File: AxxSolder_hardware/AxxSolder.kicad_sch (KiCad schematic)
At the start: 130 parts, among them IC1 OPA2387DSGT, IC3 TPS54302DDCR, IC4 STUSB4500QTR, IC5 LTC4440AHMS8E, IC6 MAX16171ATA_VY+T, IC7 STM32G431CBT6, J1 USB4110-GF-A, J2 691243110009, J3 Conn_01x05_Socket, Q1 STL9P3LLH6, Q2 2N7002NXAKR, Q3 STL10N3LLH5, U3 PEC11J-9220F-S0015, U4 BSC014N04LS

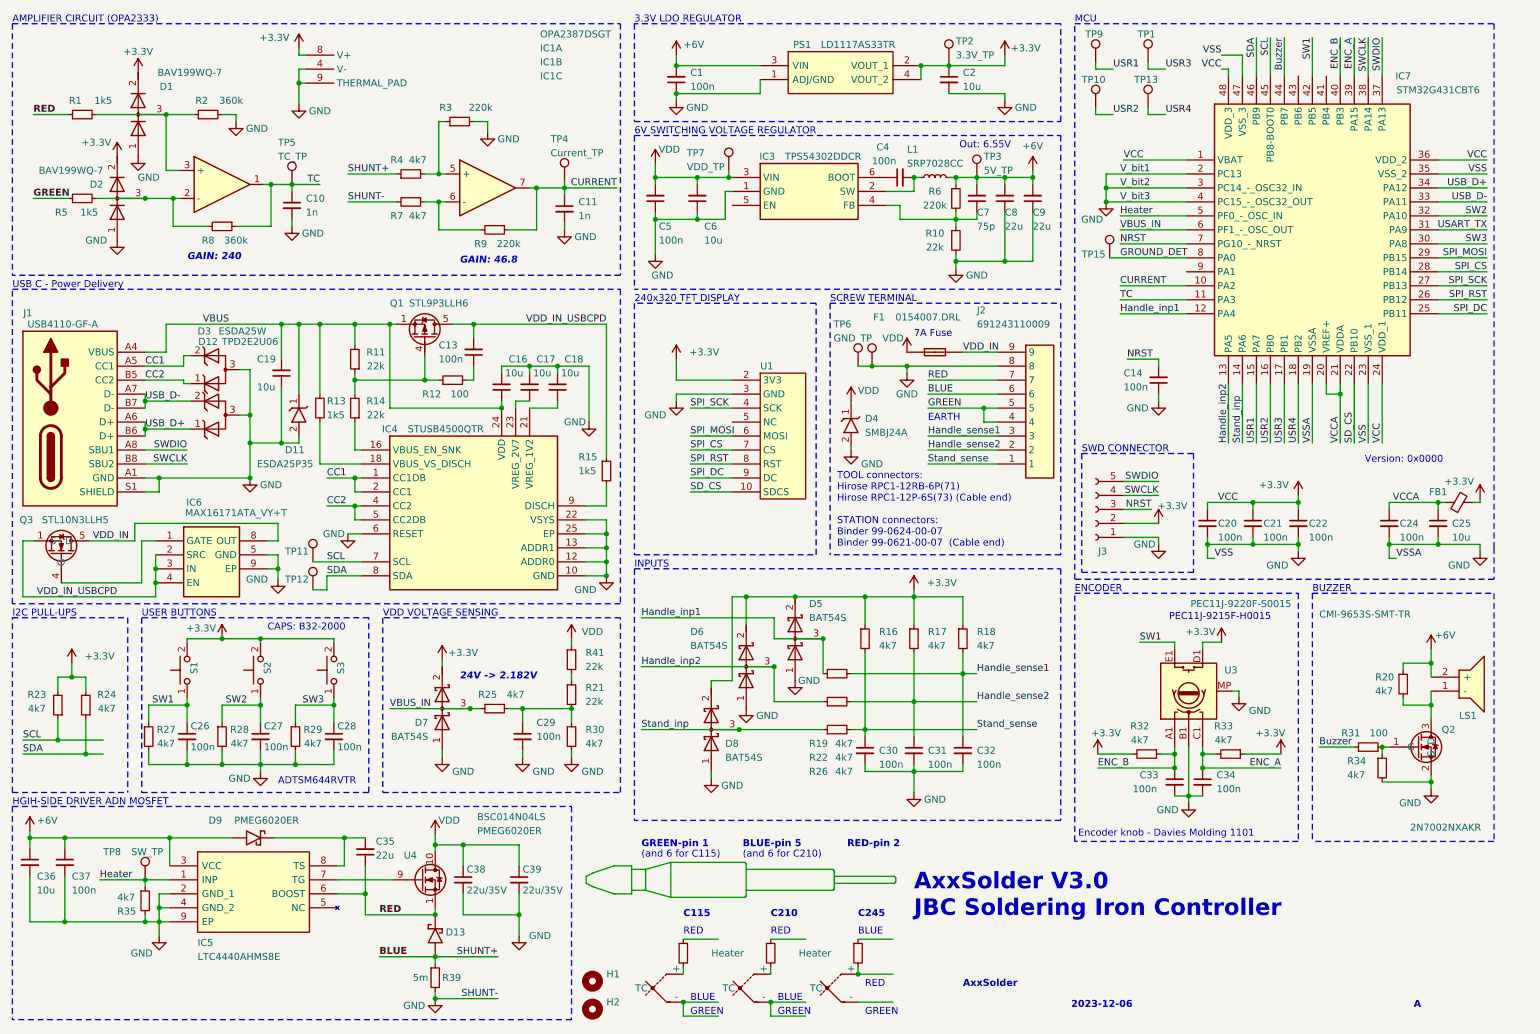
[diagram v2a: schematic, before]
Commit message: Update grounding layout and adding a fuse
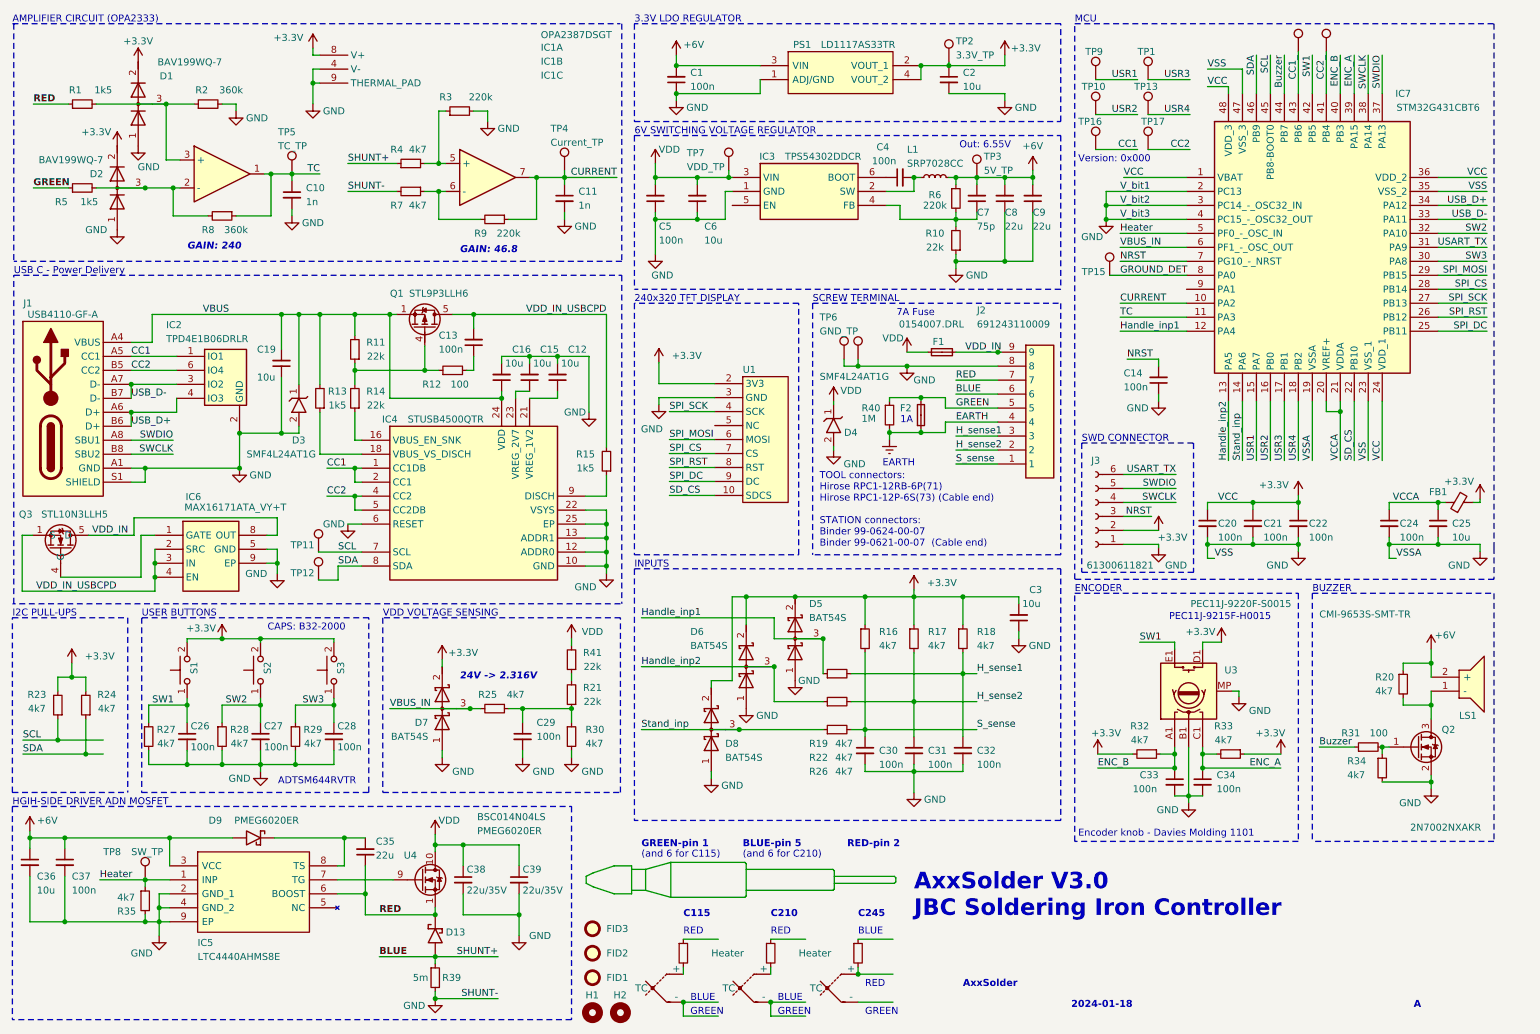
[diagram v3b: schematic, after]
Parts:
- removed C17, C18: 10u, Capacitor_SMD:C_0603_1608Metric, symbol Device:C_Small
- removed D11: ESDA25P35, footprints:ESDA25P351U1M, symbol ESDA25P35-1U1M:ESDA25P35-1U1M
- removed D12: TPD2E2U06, footprints:SOT95P237X95-3N, symbol TPD2E2U06QDBZRQ1:TPD2E2U06QDBZRQ1
- removed D3: ESDA25W, footprints:SOT65P210X110-3N, symbol ESDA25W:ESDA25W
- removed D4: SMBJ24A, footprints:DIOM5436X261N, symbol SMBJ24A:SMBJ24A
- removed J3: Conn_01x05_Socket, Connector_PinSocket_2.54mm:PinSocket_1x05_P2.54mm_Vertical, symbol Connector:Conn_01x05_Socket
- added C12, C15, C3: 10u, Capacitor_SMD:C_0603_1608Metric, symbol Device:C_Small
- added D3, D4: SMF4L24AT1G, footprints:SODFL3619X98N, symbol SMF4L24AT1G:SMF4L24AT1G
- added F2: SF-2410FP100W-2, SF2410FP100W2, symbol SF-2410FP100W-2:SF-2410FP100W-2
- added FID1, FID2, FID3: Fiducial, Fiducial:Fiducial_0.75mm_Mask1.5mm, symbol Mechanical:Fiducial
- added IC2: TPD4E1B06DRLR, footprints:SOTFL50P160X60-6N, symbol TPD4E1B06DRLR:TPD4E1B06DRLR
- added J3: 61300611821, footprints:RHDR6W97P0X254_1X6_1574X250X865P, symbol 61300611821:61300611821
- added R40: 1M, Resistor_SMD:R_1206_3216Metric, symbol Device:R_Small
- added TP16, TP17, TP18, TP19: DIAG_TP, TestPoint:TestPoint_Pad_D1.0mm, symbol Connector:TestPoint
- C16: Manufacturer_Name KEMET -> Murata Electronics; Manufacturer_Part_Number C0603C105M8PACTU -> GRM188R6YA106MA73J
- F1: footprint footprints:0154100DR -> 0154100DR
- IC7: footprint QFP50P900X900X160-48N -> footprints:QFP50P900X900X160-48N
- R10: Manufacturer_Part_Number ERJ-PB3B1332V -> ERJ-UP3J223V; Mouser Part Number 667-ERJ-PB3B1332V -> 667-ERJ-UP3J223V
- R13, R15: Manufacturer_Part_Number ERJ-H3EF1001V -> ERJ-H3ED1501V; Mouser Part Number 667-ERJ-H3EF1001V -> 667-ERJ-H3ED1501V
- R21, R41: Manufacturer_Part_Number ERJ-H3ED4702V -> ERJ-UP3J223V; Mouser Part Number 667-ERJ-H3ED4702V -> 667-ERJ-UP3J223V
- R6: Manufacturer_Part_Number ERJ-UP3D1003V -> ERJ-3RED2203V; Mouser Part Number 667-ERJ-UP3D1003V -> 667-ERJ-3RED2203V
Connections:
- net +3.3V: now also C3.2, J3.2 (Pin_2)
- net CC1: now also IC2.1 (IO1), TP16.1
- net CC2: now also IC2.6 (IO4), TP17.1
- net GND: now also R10.1, C12.2, C15.2, C3.1, D3.2 (A), D4.2 (A), IC2.2 (GND), J3.1 (Pin_1); no longer R10.2
- net GREEN: now also F2.2, R40.1; no longer J2.4
- net NRST: now also J3.3 (Pin_3)
- net SWCLK: now also J3.4 (Pin_4)
- net SWDIO: now also J3.5 (Pin_5)
- net USART_TX: now also J3.6 (Pin_6)
- net USB_D+: now also IC2.4 (IO3)
- net USB_D-: now also IC2.3 (IO2)
- net VBUS: now also R13.2, D3.1 (K); no longer R13.1
- net VDD: now also R41.2, D4.1 (K); no longer R41.1
- net VDD_IN_USBCPD: now also R15.2; no longer R15.1
- net at C7.1, IC3.4 (FB), R6.2: now also R10.2; no longer R10.1
- net at R21.1: now also C29.1, R25.1, R30.1; no longer R41.2
- net at IC4.18 (VBUS_VS_DISCH): now also R13.1; no longer R13.2
- net at IC4.23 (VREG_2V7): now also C15.1
- net at IC4.21 (VREG_1V2): now also C12.1
- net CC2_: now reaches IC7.41 (PB4)
- net CC2_: now also TP19.1
- net CC1_: now reaches IC7.43 (PB6)
- net CC1_: now also TP18.1
- net at IC4.9 (DISCH): now also R15.1; no longer R15.2
- net Handle_sense1 renamed H_sense1
- net Handle_sense2 renamed H_sense2
- net Stand_sense renamed S_sense
- new net: R21.2, R41.1
- new net Earth: F2.1, J2.4, R40.2
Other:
- note added: "1A"
- note added: "2024-01-18"
- note added: "24V -> 2.316V"
- note added: "Version: 0x000"
- note removed: "2023-12-06"
- note removed: "24V -> 2.182V"
- note removed: "Version: 0x0000"
- moved on the sheet: C10, C11, C13, C19, D1, D2, H1, H2, IC1A, IC1B, IC1C, IC4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

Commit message: Updates on PCB before ordering
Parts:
- removed TP15: DIAG_TP, TestPoint:TestPoint_Pad_D1.0mm, symbol Connector:TestPoint
- added J4, J5: TSW-102-07-T-S, footprints:TSW-102-XX-YY-S, symbol TSW-102-07-T-S:TSW-102-07-T-S
- C1, C13, C14, C20, C21, C22, C24, C26, C27, C28, C29, C30, C31, C32, C33, C34, C37, C4, C5: Mouser Part Number (none) -> 80-C0603C104J5R
- C10, C11: Mouser Part Number (none) -> 80-C0603C102K3G
- C12, C15, C16, C19, C2, C25, C3, C36, C6: Mouser Part Number (none) -> 81-GRM188R6YA106MA3J
- C35, C8, C9: Mouser Part Number (none) -> 187-CL31A226MOCLNNC
- C38, C39: Mouser Part Number (none) -> 810-C3216X5R1V226M
- C7: Mouser Part Number (none) -> 80-C0603C750K5HACTU
- D3, D4: Mouser Part Number (none) -> 576-SMF4L24AT1G
- F1: footprint 0154100DR -> footprints:0154100DR
- F2: footprint SF2410FP100W2 -> footprints:SF2410FP100W2
- Q3: footprint footprints:STL10N3LLH5 -> STL10N3LLH5
- R40: Manufacturer_Name (none) -> Bourns
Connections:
- net GROUND_DET is gone; now on net ENC_A: IC7.8 (PA0)
- net ENC_A: no longer IC7.39 (PA15)
- net SCL: now also IC7.39 (PA15); no longer IC7.45 (PB8-BOOT0)
- net SW3: now also IC7.45 (PB8-BOOT0); no longer IC7.30 (PA8)
- net USR1: now also IC7.9 (PA1); no longer IC7.15 (PA7)
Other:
- note added: "LCD"
- note added: "RIC11-31S15D7-GSMT"
- note added: "SUPPORT"
- moved on the sheet: FID2, FID3

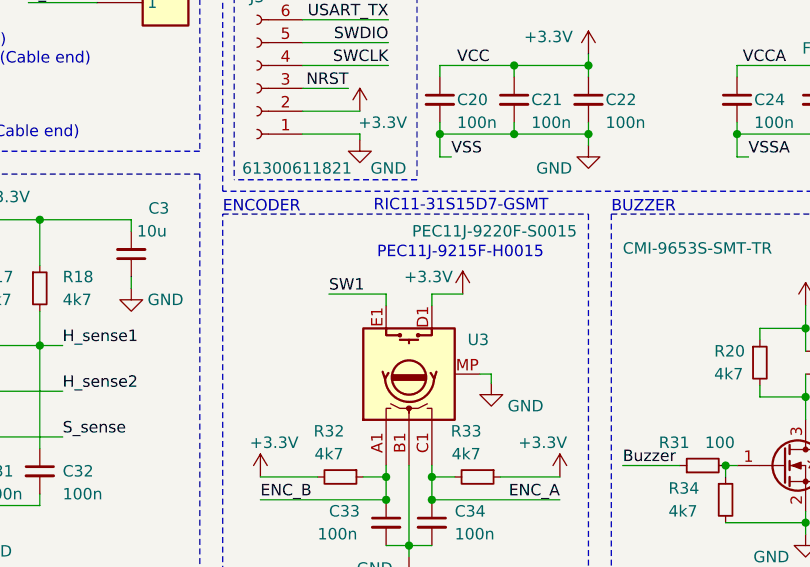
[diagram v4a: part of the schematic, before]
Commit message: update BOM and PCB dawing
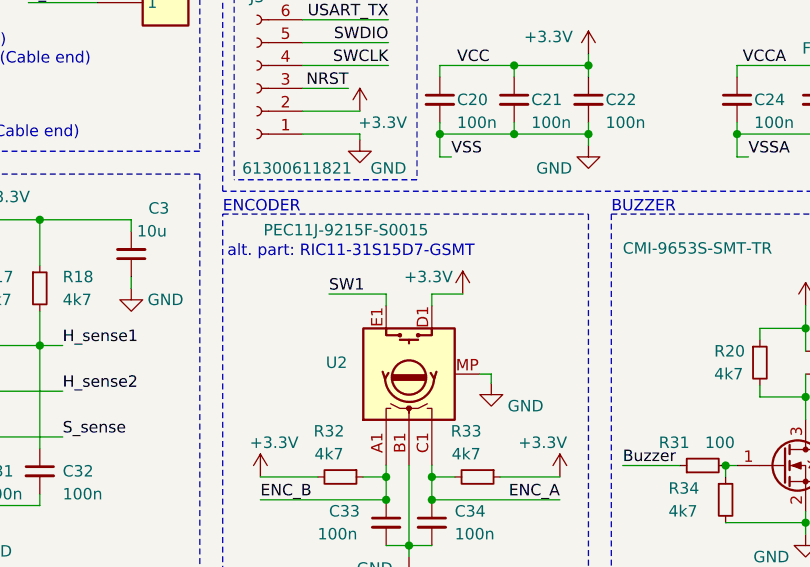
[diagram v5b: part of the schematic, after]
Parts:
- removed U3: PEC11J-9220F-S0015, footprints:PEC11J9220FS0015, symbol PEC11J-9220F-S0015:PEC11J-9220F-S0015
- added U2: PEC11J-9215F-S0015, footprints:PEC11J9215FS0015, symbol PEC11J-9215F-S0015:PEC11J-9220F-S0015
- S1, S2, S3: value ADTSM644KVTR -> ADTSM644RVTR; footprint footprints:ADTSM644KVTR -> footprints:ADTSM644RVTR; Manufacturer_Part_Number ADTSM644KVTR -> ADTSM644RVTR; Mouser Part Number 642-ADTSM644KVTR -> 642-ADTSM644RVTR; Mouser Price/Stock https://www.mouser.co.uk/ProductDetail/Apem/ADTSM644KVTR?qs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 -> (none)
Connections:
- net +3.3V: now also U2.D1
- net ENC_A: now also U2.C1
- net ENC_B: now also U2.A1
- net GND: now also U2.B1, U2.MP
- net SW1: now also U2.E1
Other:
- note added: "alt. part: RIC11-31S15D7-GSMT"
- note removed: "PEC11J-9215F-H0015"
- note removed: "RIC11-31S15D7-GSMT"
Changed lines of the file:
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@@
     (effects (font (size 1.27 1.27)) (justify left bottom))
   )
-  (text "PEC11J-9215F-H0015\n" (at 224.155 123.825 0)
-    (effects (font (size 1.27 1.27)) (justify left bottom))
-  )
   (text "C115" (at 135.89 177.8 0)
     (effects (font (size 1.27 1.27) (thickness 0.254) bold) (justify left bottom))
@@
     (effects (font (size 1.27 1.27) (color 0 132 0 1)) (justify left bottom))
   )
-  (text "RIC11-31S15D7-GSMT\n" (at 223.774 118.618 0)
+  (text "alt. part: RIC11-31S15D7-GSMT\n" (at 207.518 123.698 0)
     (effects (font (size 1.27 1.27)) (justify left bottom))
   )
@@
     )
   )
+  (symbol (lib_id "PEC11J-9215F-S0015:PEC11J-9220F-S0015") (at 227.711 146.685 90) (unit 1)
+    (in_bom yes) (on_board yes) (dnp no)
+    (property "Reference" "U2" (at 220.853 135.255 90)
+      (effects (font (size 1.27 1.27)) (justify left))
+    )
+    (property "Value" "PEC11J-9215F-S0015" (at 229.87 120.523 90)
+      (effects (font (size 1.27 1.27)) (justify left))
+    )
+    (property "Footprint" "footprints:PEC11J9215FS0015" (at 322.631 117.475 0)
+      (effects (font (size 1.27 1.27)) (justify left top) hide)
+    )
+    (property "Datasheet" "http://www.bourns.com/docs/Product-Datasheets/PEC11J.pdf" (at 422.631 117.475 0)
+      (effects (font (size 1.27 1.27)) (justify left top) hide)
+    )
+    (property "Height" "25" (at 622.631 117.475 0)
+      (effects (font (size 1.27 1.27)) (justify left top) hide)
+    )
+    (property "Mouser Part Number" "652-PEC11J9215FS0015" (at 722.631 117.475 0)
+      (effects (font (size 1.27 1.27)) (justify left top) hide)
+    )
+    (property "Manufacturer_Name" "Bourns" (at 922.631 117.475 0)
+      (effects (font (size 1.27 1.27)) (justify left top) hide)
+    )
+    (property "Manufacturer_Part_Number" "PEC11J-9215F-S0015" (at 1022.631 117.475 0)
+      (effects (font (size 1.27 1.27)) (justify left top) hide)
+    )
+    (pin "A1")
+    (pin "B1")
+    (pin "D1")
+    (pin "MP")
+    (pin "C1")
+    (pin "E1")
+    (instances
+      (project "AxxSolder"
+        (path "/d71363c3-4d90-469c-a600-831e2a7cdaef"
+          (reference "U2") (unit 1)
+        )
+      )
+    )
+  )
   (symbol (lib_id "power:GND") (at 55.245 96.012 0) (unit 1)
     (in_bom yes) (on_board yes) (dnp no)
@@
       (effects (font (size 1.27 1.27)) (justify right))
     )
-    (property "Value" "ADTSM644KVTR" (at 67.31 122.555 0)
+    (property "Value" "ADTSM644RVTR" (at 67.31 122.555 0)
       (effects (font (size 1.27 1.27)) hide)
     )
-    (property "Footprint" "footprints:ADTSM644KVTR" (at 167.31 111.125 0)
+    (property "Footprint" "footprints:ADTSM644RVTR" (at 167.31 111.125 0)
       (effects (font (size 1.27 1.27)) (justify left top) hide)
     )
@@
       (effects (font (size 1.27 1.27)) (justify left top) hide)
     )
-    (property "Mouser Part Number" "642-ADTSM644KVTR" (at 567.31 111.125 0)
-      (effects (font (size 1.27 1.27)) (justify left top) hide)
-    )
-    (property "Mouser Price/Stock" "https://www.mouser.co.uk/ProductDetail/Apem/ADTSM644KVTR?qs=iGLABakYCr8JAVbGN1VH7A%3D%3D" (at 667.31 111.125 0)
+    (property "Mouser Part Number" "642-ADTSM644RVTR" (at 567.31 111.125 0)
       (effects (font (size 1.27 1.27)) (justify left top) hide)
     )
@@
       (effects (font (size 1.27 1.27)) (justify left top) hide)
     )
-    (property "Manufacturer_Part_Number" "ADTSM644KVTR" (at 867.31 111.125 0)
+    (property "Manufacturer_Part_Number" "ADTSM644RVTR" (at 867.31 111.125 0)
       (effects (font (size 1.27 1.27)) (justify left top) hide)
     )
@@
       (effects (font (size 1.27 1.27)) (justify right))
     )
-    (property "Value" "ADTSM644KVTR" (at 40.64 122.555 0)
+    (property "Value" "ADTSM644RVTR" (at 40.64 122.555 0)
       (effects (font (size 1.27 1.27)) hide)
     )
-    (property "Footprint" "footprints:ADTSM644KVTR" (at 140.64 111.125 0)
+    (property "Footprint" "footprints:ADTSM644RVTR" (at 140.64 111.125 0)
       (effects (font (size 1.27 1.27)) (justify left top) hide)
     )
@@
       (effects (font (size 1.27 1.27)) (justify left top) hide)
     )
-    (property "Mouser Part Number" "642-ADTSM644KVTR" (at 540.64 111.125 0)
-      (effects (font (size 1.27 1.27)) (justify left top) hide)
-    )
-    (property "Mouser Price/Stock" "https://www.mouser.co.uk/ProductDetail/Apem/ADTSM644KVTR?qs=iGLABakYCr8JAVbGN1VH7A%3D%3D" (at 640.64 111.125 0)
+    (property "Mouser Part Number" "642-ADTSM644RVTR" (at 540.64 111.125 0)
       (effects (font (size 1.27 1.27)) (justify left top) hide)
     )
@@
       (effects (font (size 1.27 1.27)) (justify left top) hide)
     )
-    (property "Manufacturer_Part_Number" "ADTSM644KVTR" (at 840.64 111.125 0)
+    (property "Manufacturer_Part_Number" "ADTSM644RVTR" (at 840.64 111.125 0)
       (effects (font (size 1.27 1.27)) (justify left top) hide)
     )
@@
     )
   )
-  (symbol (lib_id "PEC11J-9220F-S0015:PEC11J-9220F-S0015") (at 227.711 146.685 90) (unit 1)
-    (in_bom yes) (on_board yes) (dnp no)
-    (property "Reference" "U3" (at 236.601 132.715 90)
-      (effects (font (size 1.27 1.27)) (justify left))
-    )
-    (property "Value" "PEC11J-9220F-S0015" (at 246.38 120.65 90)
-      (effects (font (size 1.27 1.27)) (justify left))
-    )
-    (property "Footprint" "footprints:PEC11J9220FS0015" (at 322.631 117.475 0)
-      (effects (font (size 1.27 1.27)) (justify left top) hide)
-    )
-    (property "Datasheet" "http://www.bourns.com/docs/Product-Datasheets/PEC11J.pdf" (at 422.631 117.475 0)
-      (effects (font (size 1.27 1.27)) (justify left top) hide)
-    )
-    (property "Height" "25" (at 622.631 117.475 0)
-      (effects (font (size 1.27 1.27)) (justify left top) hide)
-    )
-    (property "Mouser Part Number" "652-PEC11J9220FS0015" (at 722.631 117.475 0)
-      (effects (font (size 1.27 1.27)) (justify left top) hide)
-    )
-    (property "Mouser Price/Stock" "https://www.mouser.co.uk/ProductDetail/Bourns/PEC11J-9220F-S0015?qs=11PymoJGorKK%252Ba0mQ8KVhA%3D%3D" (at 822.631 117.475 0)
-      (effects (font (size 1.27 1.27)) (justify left top) hide)
-    )
-    (property "Manufacturer_Name" "Bourns" (at 922.631 117.475 0)
-      (effects (font (size 1.27 1.27)) (justify left top) hide)
-    )
-    (property "Manufacturer_Part_Number" "PEC11J-9220F-S0015" (at 1022.631 117.475 0)
-      (effects (font (size 1.27 1.27)) (justify left top) hide)
-    )
-    (pin "A1")
-    (pin "B1")
-    (pin "C1")
-    (pin "D1")
-    (pin "E1")
-    (pin "MP")
-    (instances
-      (project "AxxSolder"
-        (path "/d71363c3-4d90-469c-a600-831e2a7cdaef"
-          (reference "U3") (unit 1)
-        )
-      )
-    )
-  )
   (symbol (lib_id "power:+3.3V") (at 233.68 127.635 0) (unit 1)
     (in_bom yes) (on_board yes) (dnp no)
@@
       (effects (font (size 1.27 1.27)) (justify right))
     )
-    (property "Value" "ADTSM644KVTR" (at 53.975 122.555 0)
+    (property "Value" "ADTSM644RVTR" (at 53.975 122.555 0)
       (effects (font (size 1.27 1.27)) hide)
     )
-    (property "Footprint" "footprints:ADTSM644KVTR" (at 153.975 111.125 0)
+    (property "Footprint" "footprints:ADTSM644RVTR" (at 153.975 111.125 0)
       (effects (font (size 1.27 1.27)) (justify left top) hide)
     )
@@
       (effects (font (size 1.27 1.27)) (justify left top) hide)
     )
-    (property "Mouser Part Number" "642-ADTSM644KVTR" (at 553.975 111.125 0)
-      (effects (font (size 1.27 1.27)) (justify left top) hide)
-    )
-    (property "Mouser Price/Stock" "https://www.mouser.co.uk/ProductDetail/Apem/ADTSM644KVTR?qs=iGLABakYCr8JAVbGN1VH7A%3D%3D" (at 653.975 111.125 0)
+    (property "Mouser Part Number" "642-ADTSM644RVTR" (at 553.975 111.125 0)
       (effects (font (size 1.27 1.27)) (justify left top) hide)
     )
@@
       (effects (font (size 1.27 1.27)) (justify left top) hide)
     )
-    (property "Manufacturer_Part_Number" "ADTSM644KVTR" (at 853.975 111.125 0)
+    (property "Manufacturer_Part_Number" "ADTSM644RVTR" (at 853.975 111.125 0)
       (effects (font (size 1.27 1.27)) (justify left top) hide)
     )
